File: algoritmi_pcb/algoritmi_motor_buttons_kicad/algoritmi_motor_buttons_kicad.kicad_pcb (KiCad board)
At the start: 2 copper layers, 50 x 50 mm, 19 parts, among them J1 TSM-105-01-F-SH, U1 MT6701-CT

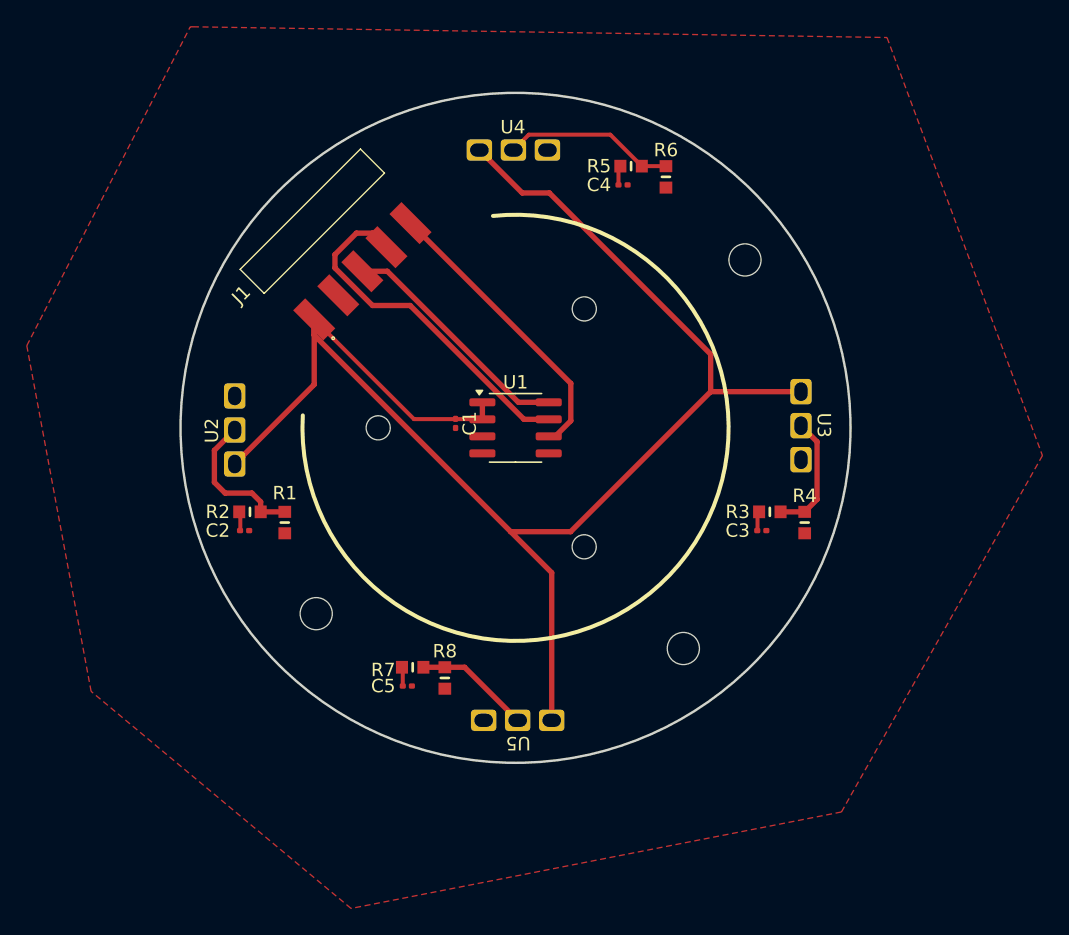
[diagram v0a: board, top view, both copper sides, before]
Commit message: generated BOMs and Gerbers
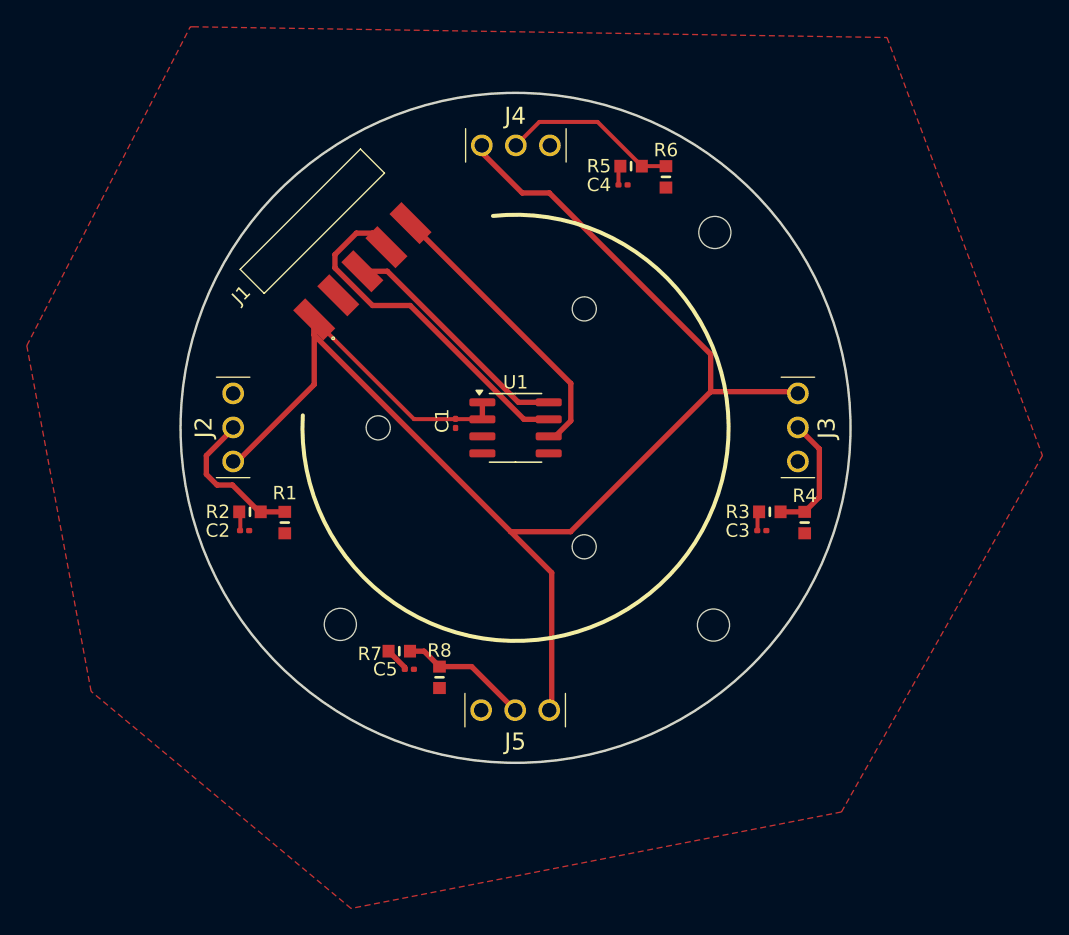
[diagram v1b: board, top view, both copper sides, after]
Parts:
- removed U2, U3, U4, U5: ~, SamacSys_Parts:microswitch
- added J2: AV4404, SamacSys_Parts:AV4404, F.Cu at (121.8, 93.2)
- added J3: AV4404, SamacSys_Parts:AV4404, F.Cu at (163.9, 88.2)
- added J4: AV4404, SamacSys_Parts:AV4404, F.Cu at (140.4, 69.7)
- added J5: AV4404, SamacSys_Parts:AV4404, F.Cu at (145.4, 111.8)
- moved R7 1.56 mm to (134.2, 107.4)
- moved C5 1.26 mm to (134.9, 108.8)
- moved R8 0.40 mm to (137.2, 109.3)
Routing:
- net Net-(J5-NO): track 8.68 -> 9.67 mm
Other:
- outline, holes or cut-outs redrawn
